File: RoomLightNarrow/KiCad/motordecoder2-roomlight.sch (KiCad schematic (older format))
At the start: 39 parts, among them P1 PAD, P2 PAD, P3 PAD, P4 PAD, P5 PAD, P6 PAD, P7 PAD, P8 PAD, P9 PROG, Q1 DMG6601LVT, Q2 DMG6601LVT, Q3 PMBT3904VS, Q5 2SC4116, Q6 PMBT3906VS, Q8 PMBT3904VS, U2 ATtiny1606-M

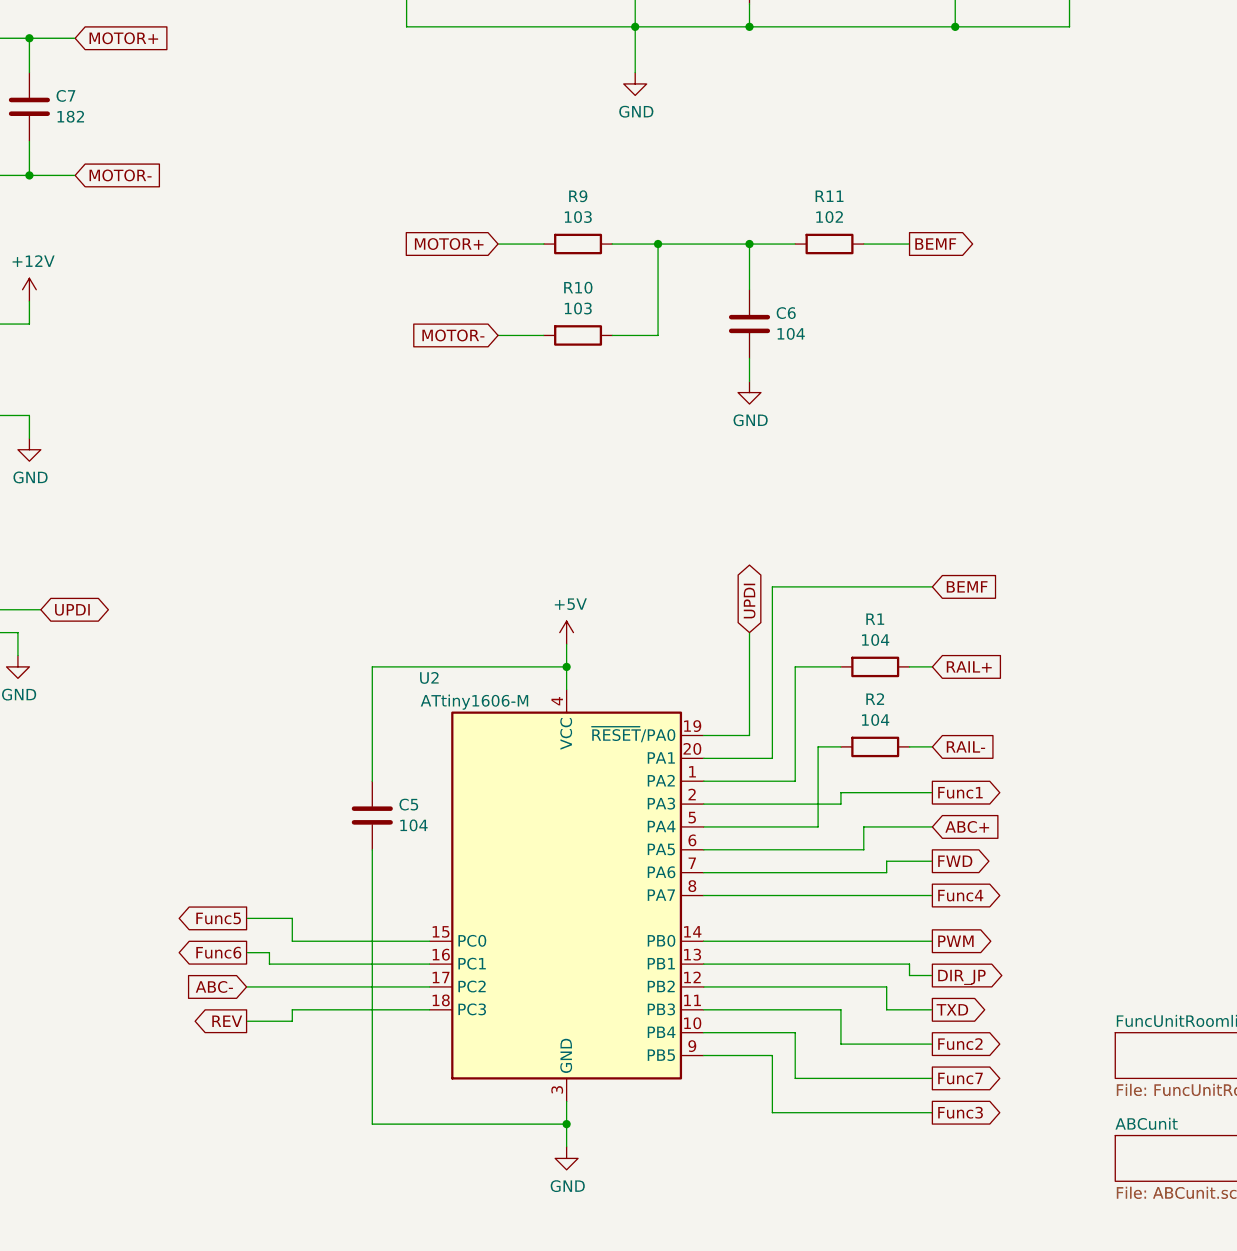
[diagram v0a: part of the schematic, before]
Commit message: 回路の問題点を修正 (K3066: Rev3 / それ以外: Rev2)
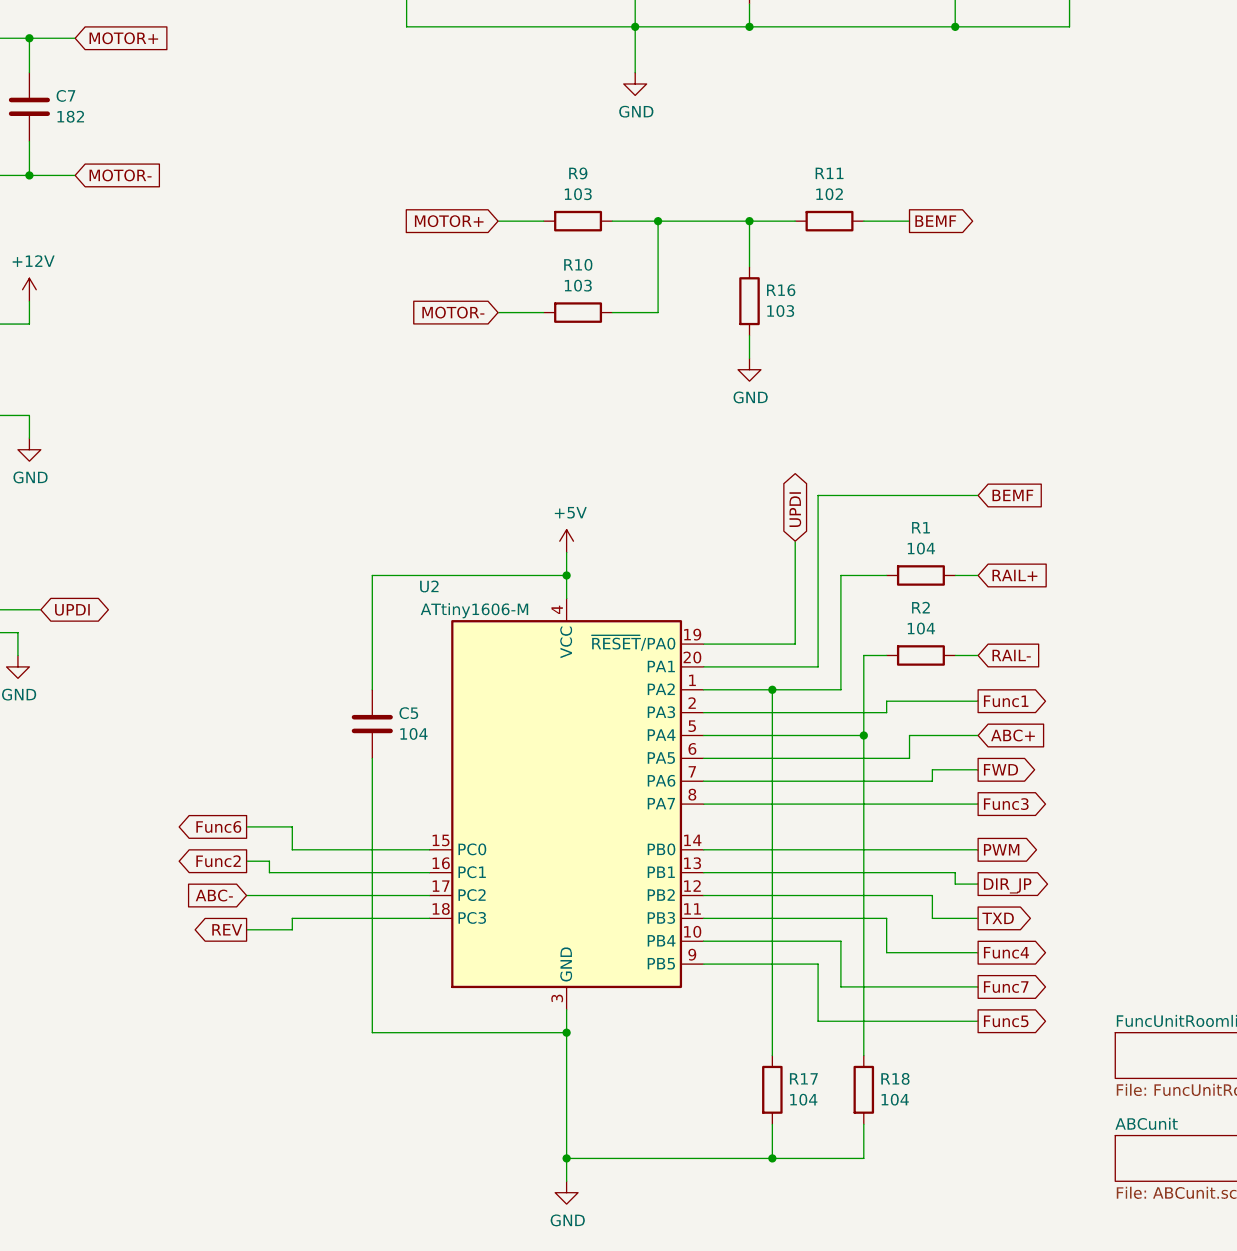
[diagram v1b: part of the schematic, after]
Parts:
- removed C6: 104, footprint:C_1005_v2, symbol Device:C
- added R16: 103, footprint:R_1005, symbol Device:R
- added R17: 104, footprint:R_1608_v2, symbol Device:R
- added R18: 104, footprint:R_1005, symbol Device:R
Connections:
- net Func2: now also U2.16 (PC1); no longer U2.11 (PB3)
- net Func3: now also U2.8 (PA7); no longer U2.9 (PB5)
- net Func4: now also U2.11 (PB3); no longer U2.8 (PA7)
- net Func5: now also U2.9 (PB5); no longer U2.15 (PC0)
- net Func6: now also U2.15 (PC0); no longer U2.16 (PC1)
- net GND: now also R16.2, R17.2, R18.2
- net at R10.1, R11.2, R9.1: now also R16.1
- net at R1.2, U2.1 (PA2): now also R17.1
- net at R2.2, U2.5 (PA4): now also R18.1
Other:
- moved on the sheet: C5, R1, R10, R11, R2, R9, U2
